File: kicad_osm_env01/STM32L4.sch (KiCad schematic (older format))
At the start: 21 parts, among them J5 Conn_02x03_Counter_Clockwise, SW5 SW_Push

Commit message: updated schematics
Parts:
- removed C58: 4.7uF, Capacitor_SMD:C_0603_1608Metric, symbol device:C
- added C? (x4): 100nF, Capacitor_SMD:C_0603_1608Metric, symbol device:C
- R16: renamed from R?; value R -> 10k
- U14: renamed from U?; footprint LQFP64 -> (none)
- gave numbers to parts that had none: 9
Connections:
- net labels added: USART4_TX, USART_RX, WKUP2
- wire segments 123 -> 135
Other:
- note added: "SWD Programming Header"
- note added: "wkup pins 2,14,16,25\n"
- note removed: "JTAG Programming Header"
- moved on the sheet: C59, C60, C61, L2, TP85

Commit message: schematics awaiting review
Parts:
- removed J5: Conn_02x03_Counter_Clockwise, Connector_PinHeader_2.54mm:PinHeader_2x03_P2.54mm_Vertical, symbol Connector:Conn_02x03_Counter_Clockwise
- added J5: Conn_01x06, symbol Connector:Conn_01x06
- added R26: 390R, symbol device:R
- R15: value R -> DNF
- gave numbers to parts that had none: 4
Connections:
- net labels added: BOOT0, GPIO10, GPIO11, GPIO12, GPIO13, GPIO14, GPIO15, GPIO7, GPIO8, GPIO9, SAI1_FS_A, SAI1_SCK_A, SAI1_SD_A, UART4_RX, UART4_TX
- net labels removed: USART4_TX, USART_RX
- wire segments 135 -> 151
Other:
- note added: "Note: For comfirmation of pin functions refer to datasheet. Symbol may not be correct\n- wkup pins 2,14,16,25\n-pa13, pa15, pb4 avoid as after reset internal pull up and pull down activated"
- note removed: "Note: For comfirmation of pin functions refer to datasheet. Symbol may not be correct\n"
- note removed: "wkup pins 2,14,16,25\n"
- moved on the sheet: C1, C12, C13, C27, C62, D8, R119, R15, R16, R6, SW5, U14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

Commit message: rough layout with throwdown of parts
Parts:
- removed SW5: SW_Push, Button_Switch_SMD:SW_SPST_B3U-1000P, symbol Switch:SW_Push
- removed TP85: Test_Point, TestPoint:TestPoint_THTPad_D1.0mm_Drill0.5mm, symbol OSM_env01-rescue:Test_Point-Connector-ESP32-EVB_Rev_D-rescue
- added R30: 0R, Resistor_SMD:R_0402_1005Metric, symbol device:R
- added S1: B3U-1100P, Button_Switch_SMD:SW_SPST_B3U-1100P, symbol Devtank:B3U-1100P
- C1, C12, C13, C27: footprint (none) -> Capacitor_SMD:C_0402_1005Metric
- C28, C29, C30, C44, C59, C60, C61, C62: footprint Capacitor_SMD:C_0603_1608Metric -> Capacitor_SMD:C_0402_1005Metric
- D8: footprint (none) -> Devtank_PCB_lib:LED_Rectangular_W4.5mm_H7.3mm_Horizontal_2.54mm_Z3.0mm
- J5: footprint (none) -> Connector:Tag-Connect_TC2030-IDC-NL_2x03_P1.27mm_Vertical
- L2: footprint Inductor_SMD:L_0805_2012Metric -> Inductor_SMD:L_0402_1005Metric
- R119: footprint Resistor_SMD:R_0603_1608Metric -> Resistor_SMD:R_0402_1005Metric
- R15, R16: footprint (none) -> Resistor_SMD:R_0402_1005Metric
- R26, R6: footprint (none) -> Resistor_SMD:R_0603_1608Metric
- U14: footprint (none) -> Package_QFP:LQFP-64_10x10mm_P0.5mm
- Y1: footprint (none) -> Crystal:Crystal_SMD_Abracon_ABM3C-4Pin_5.0x3.2mm
- Y2: footprint (none) -> Crystal:Crystal_SMD_7050-4Pin_7.0x5.0mm
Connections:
- net ADC1: no longer U14.8 (PC0/ADC1_IN1/ADC2_IN1/ADC3_IN1/DFSDM_DATIN4/I2C3_SCL/LCD_SEG18/LPTIM1_IN1/LPTIM2_IN1/LPUART1_RX)
- net ADC2: now also U14.15 (ADC1_IN6/ADC2_IN6/LCD_SEG0/OPAMP1_VINM/TIM15_CH1N/TIM2_CH2/TIM5_CH2/UART4_RX/USART2_DE/USART2_RTS/PA1); no longer U14.9 (PC1/ADC1_IN2/ADC2_IN2/ADC3_IN2/DFSDM_CKIN4/I2C3_SDA/LCD_SEG19/LPTIM1_OUT/LPUART1_TX)
- net GND: now also R30.2, S1.1; no longer Y2.2, Y2.3
- net GPIO5: now also U14.9 (PC1/ADC1_IN2/ADC2_IN2/ADC3_IN2/DFSDM_CKIN4/I2C3_SDA/LCD_SEG19/LPTIM1_OUT/LPUART1_TX); no longer U14.51 (PC10/LCD_COM4/LCD_SEG28/LCD_SEG40/SAI2_SCK_B/SDMMC1_D2/SPI3_SCK/TSC_G3_IO2/UART4_TX/USART3_TX)
- net GPIO6: now also U14.55 (COMP2_INM/LCD_SEG7/SAI1_SCK_B/SPI1_SCK/SPI3_SCK/SYS_JTDO-SWO/TIM2_CH2/USART1_DE/USART1_RTS/PB3); no longer U14.52 (PC11/ADC1_EXTI11/ADC2_EXTI11/ADC3_EXTI11/LCD_COM5/LCD_SEG29/LCD_SEG41/SAI2_MCLK_B/SDMMC1_D3/SPI3_MISO/TSC_G3_IO3/UART4_RX/USART3_RX)
- net STM_NRST: now also S1.2
- net UART4_RX: now also U14.52 (PC11/ADC1_EXTI11/ADC2_EXTI11/ADC3_EXTI11/LCD_COM5/LCD_SEG29/LCD_SEG41/SAI2_MCLK_B/SDMMC1_D3/SPI3_MISO/TSC_G3_IO3/UART4_RX/USART3_RX); no longer U14.15 (ADC1_IN6/ADC2_IN6/LCD_SEG0/OPAMP1_VINM/TIM15_CH1N/TIM2_CH2/TIM5_CH2/UART4_RX/USART2_DE/USART2_RTS/PA1)
- net UART4_TX: now also U14.51 (PC10/LCD_COM4/LCD_SEG28/LCD_SEG40/SAI2_SCK_B/SDMMC1_D2/SPI3_SCK/TSC_G3_IO2/UART4_TX/USART3_TX); no longer U14.14 (ADC1_IN5/ADC2_IN5/OPAMP1_VINP/RTC_TAMP2/SAI1_EXTCLK/SYS_WKUP1/TIM2_CH1/TIM2_ETR/TIM5_CH1/TIM8_ETR/UART4_TX/USART2_CTS/PA0)
- net status_led: now also U14.14 (ADC1_IN5/ADC2_IN5/OPAMP1_VINP/RTC_TAMP2/SAI1_EXTCLK/SYS_WKUP1/TIM2_CH1/TIM2_ETR/TIM5_CH1/TIM8_ETR/UART4_TX/USART2_CTS/PA0); no longer U14.55 (COMP2_INM/LCD_SEG7/SAI1_SCK_B/SPI1_SCK/SPI3_SCK/SYS_JTDO-SWO/TIM2_CH2/USART1_DE/USART1_RTS/PB3)
- new net: R30.1, S1.3
- new net ADC7: U14.8 (PC0/ADC1_IN1/ADC2_IN1/ADC3_IN1/DFSDM_DATIN4/I2C3_SCL/LCD_SEG18/LPTIM1_IN1/LPTIM2_IN1/LPUART1_RX)
- no-connect marks 1 -> 3
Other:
- note removed: "make sure LED polarity is correct"
- moved on the sheet: C28, C59, C62

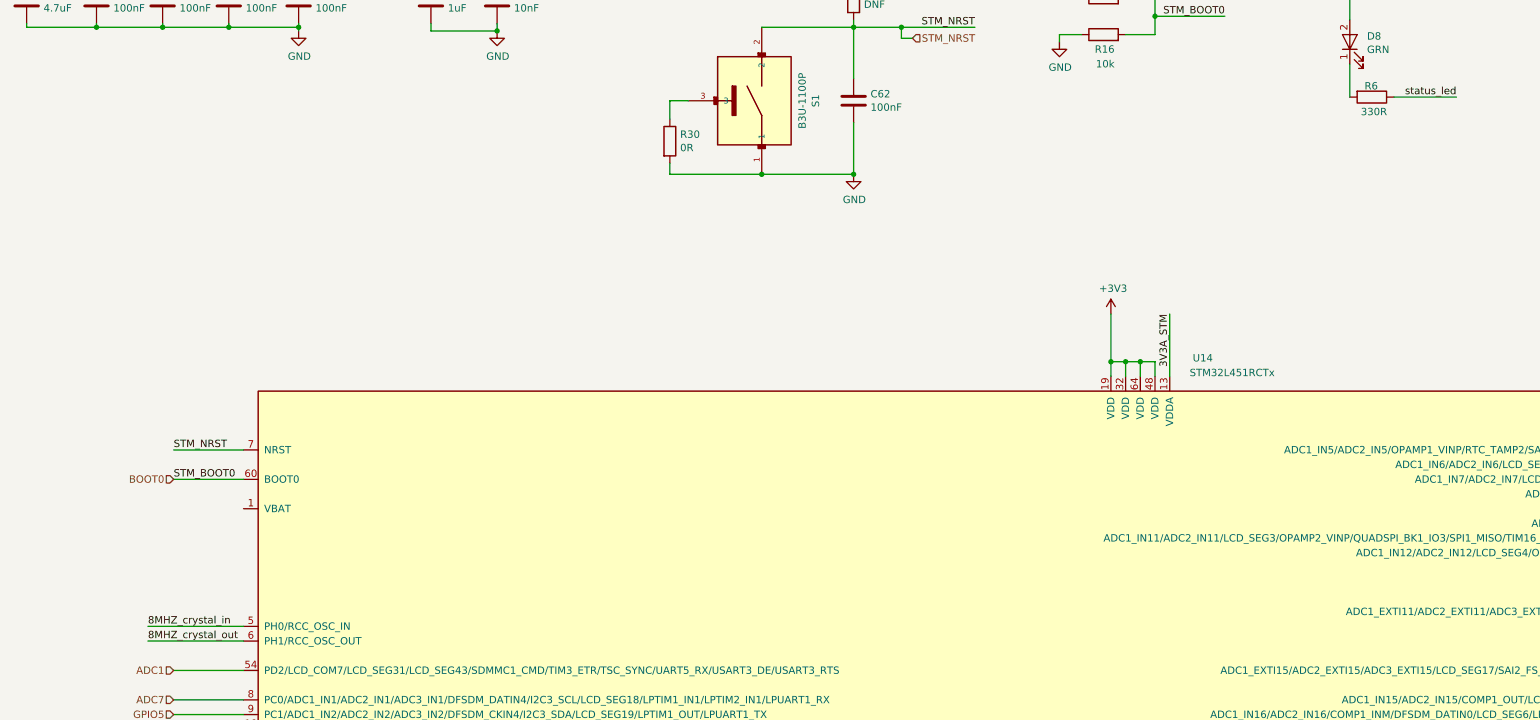
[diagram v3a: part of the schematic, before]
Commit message: updated schematics
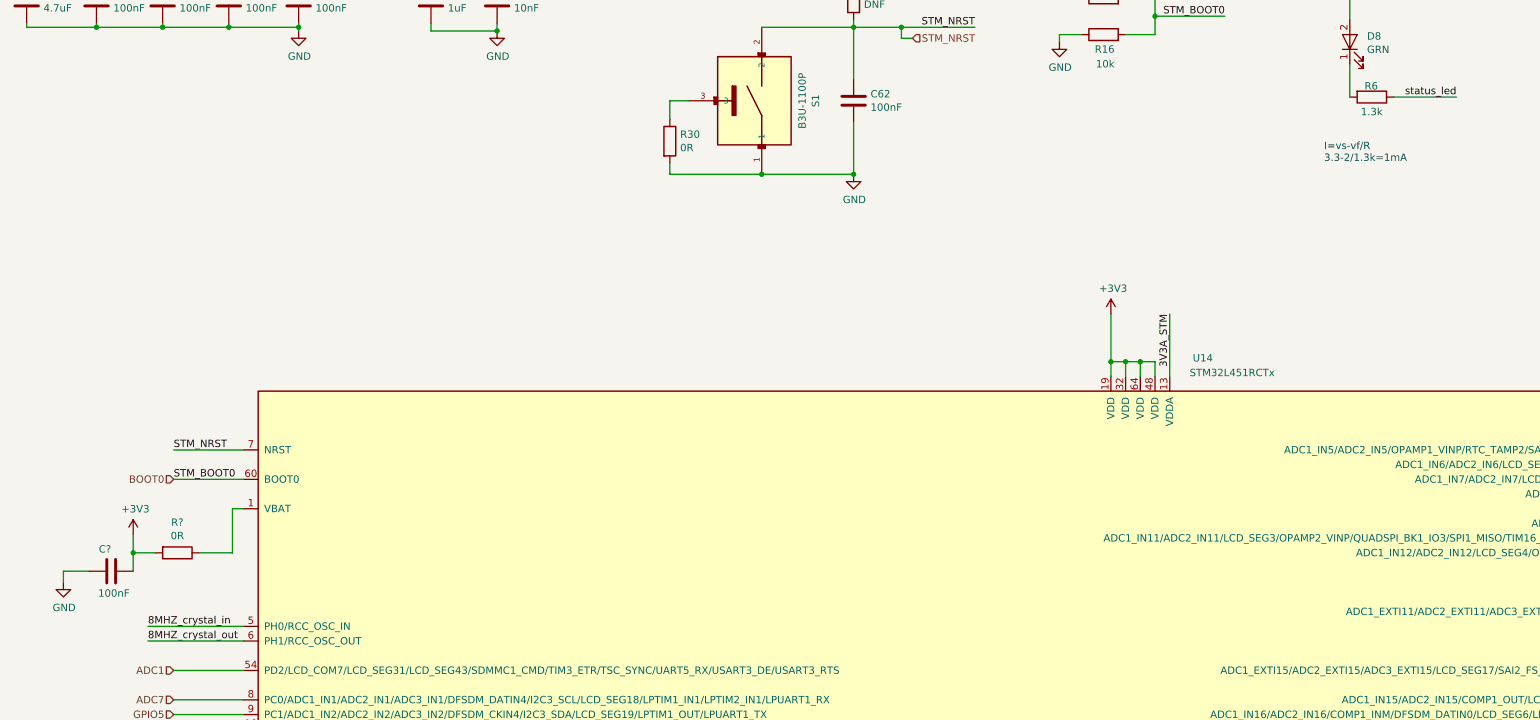
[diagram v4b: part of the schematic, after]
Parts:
- added C?: 100nF, Capacitor_SMD:C_0402_1005Metric, symbol device:C
- added R?: 0R, symbol device:R
- R6: value 330R -> 1.3k
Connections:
- net +3V3: now also C?.2, R?.2
- net GND: now also C?.1
- net at U14.1 (VBAT): now also R?.1
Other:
- note added: "I=vs-vf/R\n3.3-2/1.3k=1mA"
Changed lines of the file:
@@
-$Comp
-L device:C C?
-U 1 1 60931F37
-P 675 1150
-AR Path="/60931F37" Ref="C?"  Part="1"
-AR Path="/60917DD5/60931F37" Ref="C59"  Part="1"
-F 0 "C59" H 790 1196 50  0000 L CNN
-F 1 "4.7uF" H 790 1105 50  0000 L CNN
-F 2 "Capacitor_SMD:C_0402_1005Metric" H 713 1000 50  0001 C CNN
-F 3 "" H 675 1150 50  0001 C CNN
-	1    675  1150
-	1    0    0    -1
-$EndComp
 $Comp
 L device:C C?
@@
 $Comp
 L power:+3V3 #PWR?
-U 1 1 60947709
-P 675 900
-AR Path="/60947709" Ref="#PWR?"  Part="1"
-AR Path="/60917DD5/60947709" Ref="#PWR0111"  Part="1"
-F 0 "#PWR0111" H 675 750 50  0001 C CNN
-F 1 "+3V3" H 690 1073 50  0000 C CNN
-F 2 "" H 675 900 50  0001 C CNN
-F 3 "" H 675 900 50  0001 C CNN
-	1    675  900
-	1    0    0    -1
-$EndComp
-Wire Wire Line
-	675  1000 675  900
-$Comp
-L power:+3V3 #PWR?
 U 1 1 60948D20
 P 8050 3275
@@
 	1    9675 1425
 	0    -1   -1   0
-$EndComp
-$Comp
-L device:R R6
-U 1 1 614C56B3
-P 9825 1800
-F 0 "R6" V 9750 1750 50  0000 L CNN
-F 1 "330R" V 9925 1725 50  0000 L CNN
-F 2 "Resistor_SMD:R_0603_1608Metric" V 9755 1800 50  0001 C CNN
-F 3 "" H 9825 1800 50  0001 C CNN
-	1    9825 1800
-	0    1    1    0
 $EndComp
 Wire Wire Line
@@
 $EndComp
 Connection ~ 2050 1000
-Wire Wire Line
-	675  1000 1150 1000
 Connection ~ 1150 1000
 Wire Wire Line
@@
 Wire Wire Line
 	2525 1325 2050 1325
-Wire Wire Line
-	675  1325 675  1300
 Connection ~ 2525 1325
 Wire Wire Line
@@
 Wire Wire Line
 	1150 1300 1150 1325
-Connection ~ 1150 1325
-Wire Wire Line
-	1150 1325 675  1325
 Wire Wire Line
 	1600 1300 1600 1325
@@
 Wire Wire Line
 	2525 1000 2925 1000
-Connection ~ 675  1000
 NoConn ~ 14475 1375
 NoConn ~ 14075 1375
@@
 Wire Wire Line
 	5675 2325 6300 2325
+Text Notes 9500 2250 0    50   ~ 0
+I=vs-vf/R\n3.3-2/1.3k=1mA
+Connection ~ 1150 1325
+Wire Wire Line
+	675  1325 675  1300
+Wire Wire Line
+	675  1000 1150 1000
+Connection ~ 675  1000
+$Comp
+L device:C C?
+U 1 1 60931F37
+P 675 1150
+AR Path="/60931F37" Ref="C?"  Part="1"
+AR Path="/60917DD5/60931F37" Ref="C59"  Part="1"
+F 0 "C59" H 790 1196 50  0000 L CNN
+F 1 "4.7uF" H 790 1105 50  0000 L CNN
+F 2 "Capacitor_SMD:C_0402_1005Metric" H 713 1000 50  0001 C CNN
+F 3 "" H 675 1150 50  0001 C CNN
+	1    675  1150
+	1    0    0    -1
+$EndComp
+Wire Wire Line
+	675  1000 675  900
+$Comp
+L power:+3V3 #PWR?
+U 1 1 60947709
+P 675 900
+AR Path="/60947709" Ref="#PWR?"  Part="1"
+AR Path="/60917DD5/60947709" Ref="#PWR0111"  Part="1"
+F 0 "#PWR0111" H 675 750 50  0001 C CNN
+F 1 "+3V3" H 690 1073 50  0000 C CNN
+F 2 "" H 675 900 50  0001 C CNN
+F 3 "" H 675 900 50  0001 C CNN
+	1    675  900
+	1    0    0    -1
+$EndComp
+$Comp
+L device:R R6
+U 1 1 614C56B3
+P 9825 1800
+F 0 "R6" V 9750 1750 50  0000 L CNN
+F 1 "1.3k" V 9925 1725 50  0000 L CNN
+F 2 "Resistor_SMD:R_0603_1608Metric" V 9755 1800 50  0001 C CNN
+F 3 "" H 9825 1800 50  0001 C CNN
+	1    9825 1800
+	0    1    1    0
+$EndComp
+Wire Wire Line
+	1150 1325 675  1325
+$Comp
+L device:C C?
+U 1 1 618D4BAE
+P 1250 5025
+AR Path="/618D4BAE" Ref="C?"  Part="1"
+AR Path="/60917DD5/618D4BAE" Ref="C?"  Part="1"
+F 0 "C?" V 1400 5025 50  0000 L CNN
+F 1 "100nF" V 1100 4900 50  0000 L CNN
+F 2 "Capacitor_SMD:C_0402_1005Metric" H 1288 4875 50  0001 C CNN
+F 3 "" H 1250 5025 50  0001 C CNN
+	1    1250 5025
+	0    -1   -1   0
+$EndComp
+$Comp
+L OSM_env01:GND #PWR?
+U 1 1 618EC5A0
+P 925 5100
+F 0 "#PWR?" H 925 4850 50  0001 C CNN
+F 1 "GND" H 930 4927 50  0000 C CNN
+F 2 "" H 925 5100 60  0000 C CNN
+F 3 "" H 925 5100 60  0000 C CNN
+	1    925  5100
+	1    0    0    -1
+$EndComp
+$Comp
+L power:+3V3 #PWR?
+U 1 1 618ECC9F
+P 1400 4775
+F 0 "#PWR?" H 1400 4625 50  0001 C CNN
+F 1 "+3V3" H 1415 4948 50  0000 C CNN
+F 2 "" H 1400 4775 50  0001 C CNN
+F 3 "" H 1400 4775 50  0001 C CNN
+	1    1400 4775
+	1    0    0    -1
+$EndComp
+Wire Wire Line
+	1400 5025 1400 4900
+Wire Wire Line
+	925  5100 925  5025
+Wire Wire Line
+	925  5025 1100 5025
+Wire Wire Line
+	1400 4900 1550 4900
+Wire Wire Line
+	2075 4600 2150 4600
+Connection ~ 1400 4900
+Wire Wire Line
+	1400 4900 1400 4775
+$Comp
+L device:R R?
+U 1 1 6197C87D
+P 1700 4900
+F 0 "R?" V 1493 4900 50  0000 C CNN
+F 1 "0R" V 1584 4900 50  0000 C CNN
+F 2 "" V 1630 4900 50  0001 C CNN
+F 3 "" H 1700 4900 50  0001 C CNN
+	1    1700 4900
+	0    1    1    0
+$EndComp
+Wire Wire Line
+	1850 4900 2075 4900
+Wire Wire Line
+	2075 4600 2075 4900
 $EndSCHEMATC

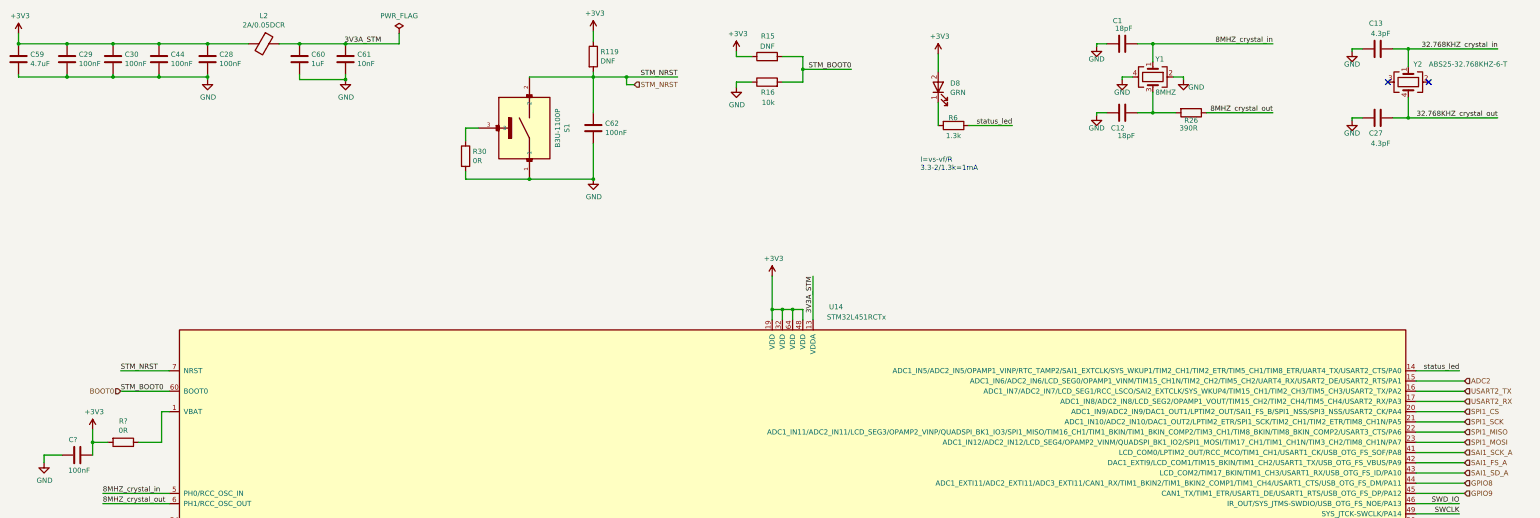
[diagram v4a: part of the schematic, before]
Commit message: updated schematics
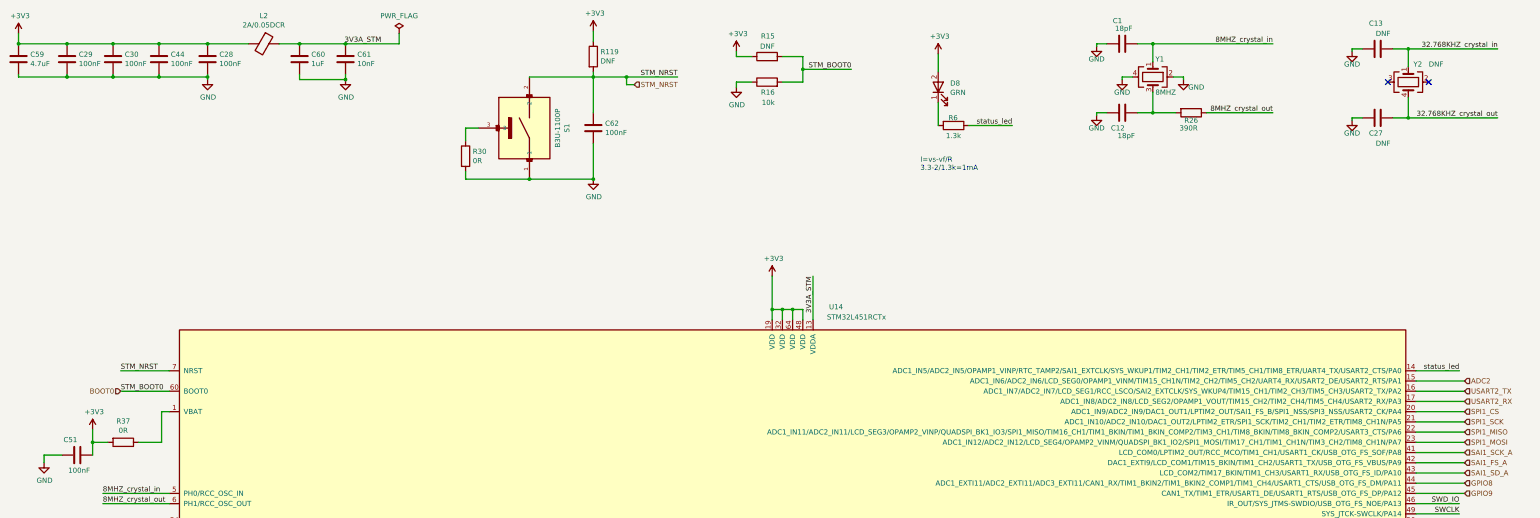
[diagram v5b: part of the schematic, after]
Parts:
- C13, C27: value 4.3pF -> DNF
- Y2: value ABS25-32.768KHZ-6-T -> DNF
- gave numbers to parts that had none: 2
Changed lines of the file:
@@
 $Descr A3 16535 11693
 encoding utf-8
-Sheet 8 9
+Sheet 6 9
 Title ""
 Date ""
@@
 P 14275 1375
 F 0 "Y2" V 14100 1425 50  0000 L CNN
-F 1 "ABS25-32.768KHZ-6-T" V 14100 1575 50  0000 L CNN
+F 1 "DNF" V 14100 1575 50  0000 L CNN
 F 2 "Crystal:Crystal_SMD_7050-4Pin_7.0x5.0mm" H 14275 1375 50  0001 C CNN
 F 3 "" H 14275 1375 50  0001 C CNN
@@
 P 13975 1725
 F 0 "C27" V 13825 1675 50  0000 L CNN
-F 1 "4.3pF" V 13725 1600 50  0000 L CNN
+F 1 "DNF" V 13725 1600 50  0000 L CNN
 F 2 "Capacitor_SMD:C_0402_1005Metric" H 14013 1575 50  0001 C CNN
 F 3 "" H 13975 1725 50  0001 C CNN
@@
 P 13975 1050
 F 0 "C13" V 14225 1000 50  0000 L CNN
-F 1 "4.3pF" V 14125 925 50  0000 L CNN
+F 1 "DNF" V 14125 925 50  0000 L CNN
 F 2 "Capacitor_SMD:C_0402_1005Metric" H 14013 900 50  0001 C CNN
 F 3 "" H 13975 1050 50  0001 C CNN
@@
 Wire Wire Line
 	675  1325 675  1300
-Wire Wire Line
-	675  1000 1150 1000
 Connection ~ 675  1000
 $Comp
@@
 P 1250 5025
 AR Path="/618D4BAE" Ref="C?"  Part="1"
-AR Path="/60917DD5/618D4BAE" Ref="C?"  Part="1"
-F 0 "C?" V 1400 5025 50  0000 L CNN
+AR Path="/60917DD5/618D4BAE" Ref="C51"  Part="1"
+F 0 "C51" V 1400 5025 50  0000 L CNN
 F 1 "100nF" V 1100 4900 50  0000 L CNN
 F 2 "Capacitor_SMD:C_0402_1005Metric" H 1288 4875 50  0001 C CNN
@@
 $EndComp
 $Comp
-L OSM_env01:GND #PWR?
+L OSM_env01:GND #PWR0127
 U 1 1 618EC5A0
 P 925 5100
-F 0 "#PWR?" H 925 4850 50  0001 C CNN
+F 0 "#PWR0127" H 925 4850 50  0001 C CNN
 F 1 "GND" H 930 4927 50  0000 C CNN
 F 2 "" H 925 5100 60  0000 C CNN
@@
 $EndComp
 $Comp
-L power:+3V3 #PWR?
+L power:+3V3 #PWR0132
 U 1 1 618ECC9F
 P 1400 4775
-F 0 "#PWR?" H 1400 4625 50  0001 C CNN
+F 0 "#PWR0132" H 1400 4625 50  0001 C CNN
 F 1 "+3V3" H 1415 4948 50  0000 C CNN
 F 2 "" H 1400 4775 50  0001 C CNN
@@
 	1400 4900 1400 4775
 $Comp
-L device:R R?
+L device:R R37
 U 1 1 6197C87D
 P 1700 4900
-F 0 "R?" V 1493 4900 50  0000 C CNN
+F 0 "R37" V 1493 4900 50  0000 C CNN
 F 1 "0R" V 1584 4900 50  0000 C CNN
 F 2 "" V 1630 4900 50  0001 C CNN
@@
 Wire Wire Line
 	2075 4600 2075 4900
+Wire Wire Line
+	675  1000 1150 1000
 $EndSCHEMATC
